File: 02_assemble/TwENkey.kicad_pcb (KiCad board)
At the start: 2 copper layers, 304.4 x 98.8 mm, 149 parts, among them J1 Conn_01x02, SW1 RotaryEncoder_Switch, SW10 SW_PUSH, SW11 SW_PUSH, SW12 SW_PUSH, SW13 SW_PUSH, SW14 SW_PUSH, SW15 SW_PUSH, SW16 SW_PUSH, SW17 SW_PUSH, SW18 SW_PUSH, SW19 SW_PUSH, SW2 SW_PUSH, SW20 SW_PUSH, SW21 SW_PUSH, SW22 SW_PUSH, SW23 SW_PUSH, SW24 SW_PUSH, SW25 SW_PUSH, SW26 SW_PUSH, SW27 SW_PUSH, SW28 SW_PUSH, SW29 SW_PUSH, SW3 SW_PUSH, SW30 SW_PUSH, SW31 SW_PUSH, SW32 SW_PUSH, SW33 SW_PUSH, SW34 SW_PUSH, SW35 SW_PUSH, SW36 SW_PUSH, SW37 SW_PUSH, SW38 SW_PUSH, SW39 SW_PUSH, SW4 SW_PUSH, SW40 SW_PUSH, SW41 SW_PUSH, SW42 SW_PUSH, SW43 SW_PUSH, SW44 SW_PUSH, SW45 SW_PUSH, SW46 SW_PUSH, SW47 SW_PUSH, SW48 SW_PUSH, SW49 SW_PUSH, SW5 SW_PUSH, SW50 SW_PUSH, SW51 SW_PUSH, SW52 SW_PUSH, SW53 SW_PUSH, SW54 SW_PUSH, SW55 SW_PUSH, SW56 SW_PUSH, SW57 SW_PUSH, SW58 SW_PUSH, SW59 SW_PUSH, SW6 SW_PUSH, SW60 SW_PUSH, SW61 SW_PUSH, SW62 SW_PUSH, SW63 SW_PUSH, SW64 SW_PUSH, SW65 SW_PUSH, SW66 SW_PUSH, SW67 SW_PUSH, SW68 SW_PUSH, SW69 SW_PUSH, SW7 SW_PUSH, SW70 SW_PUSH, SW71 SW_PUSH, SW72 SW_PUSH, SW8 SW_PUSH, SW9 SW_PUSH, U1 Micon_BLEMicroPro

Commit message: サリチル酸さんのレビューを受けて修正
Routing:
- net Row1: track 345.2 -> 384.0 mm, vias 0 -> 1
- net Row3: track 367.0 -> 395.1 mm
- net Row0: track 337.3 -> 362.4 mm, vias 2 -> 4
- net Row4: track 383.2 -> 401.0 mm
- net Row2: track 355.9 -> 372.4 mm
- net Net-(D58-Pad1): track 13.4 -> 23.3 mm
- net Net-(D69-Pad1): track 13.8 -> 19.9 mm, vias 2 -> 0
- net Net-(D63-Pad1): track 10.9 -> 16.6 mm
- net Net-(D59-Pad1): track 15.0 -> 20.3 mm
- net Net-(D70-Pad1): track 14.1 -> 18.8 mm
- net Net-(D53-Pad1): track 16.3 -> 19.9 mm
- net Net-(D60-Pad1): track 15.0 -> 18.6 mm
- net Net-(D43-Pad1): track 14.3 -> 17.4 mm
- net Col6: track 391.9 -> 394.3 mm
- net Net-(D48-Pad1): track 20.7 -> 22.6 mm
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
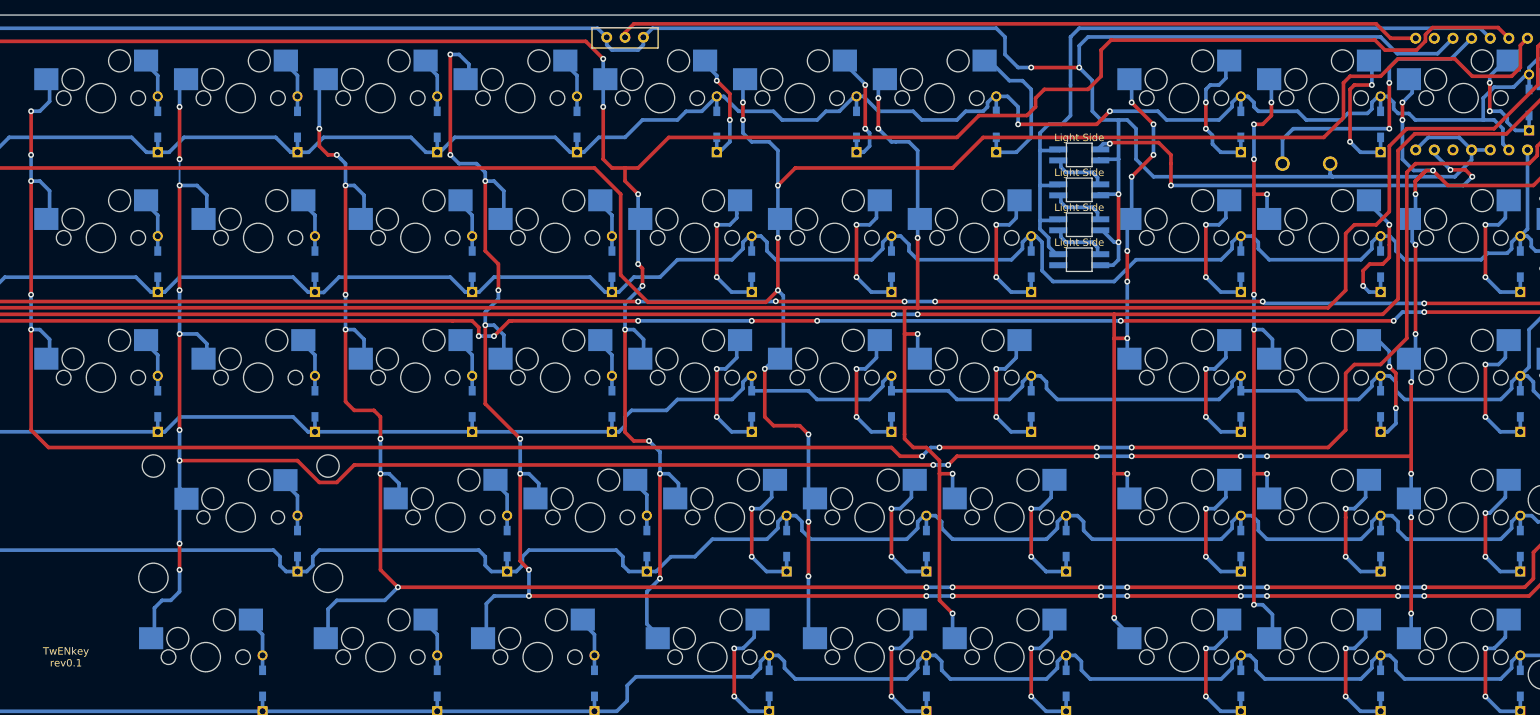
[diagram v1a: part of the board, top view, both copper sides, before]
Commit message: TRRSコネクタを追加
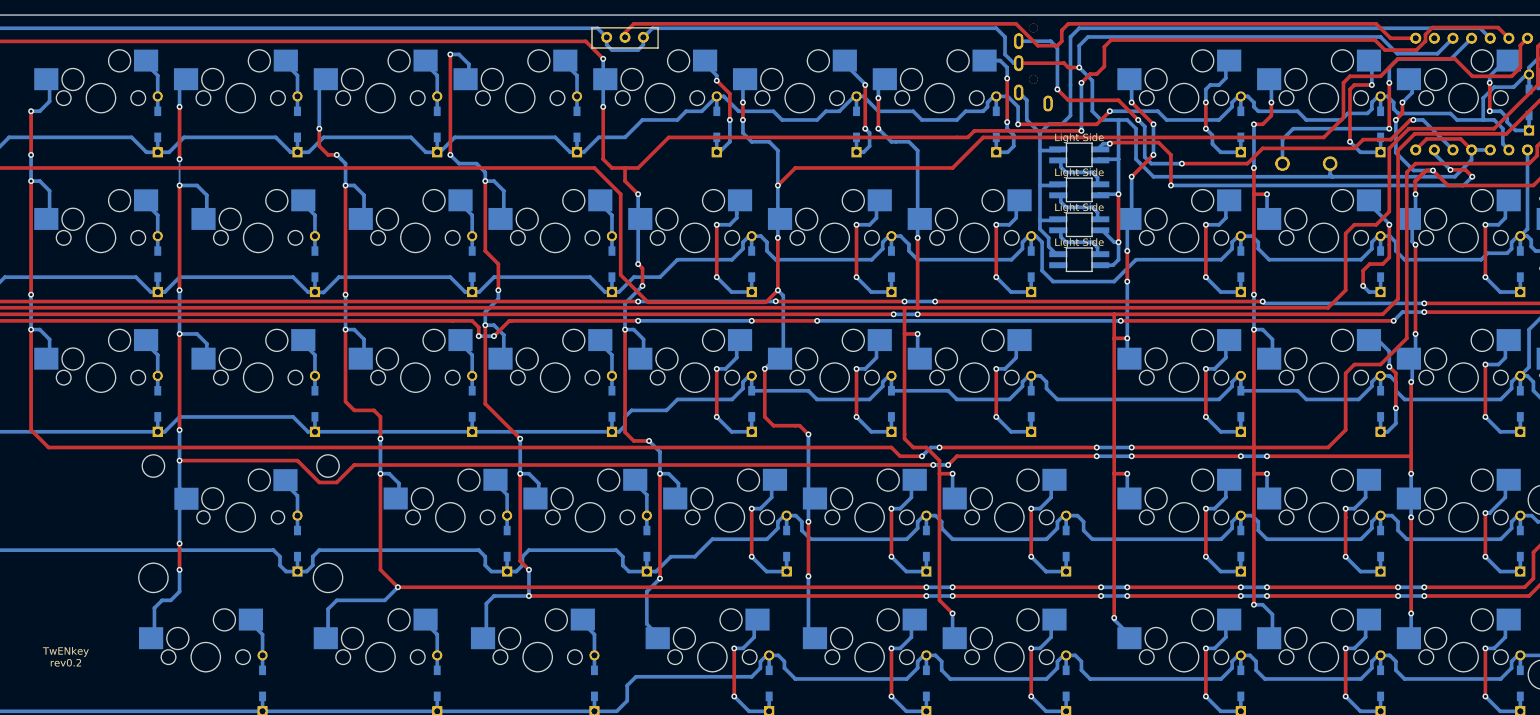
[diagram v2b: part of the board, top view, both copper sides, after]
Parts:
- added J2: MJ-4PP-9, kbd_Parts:TRRS_MJ-4PP-9, F.Cu at (236.6, 23.5)
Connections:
- U1 pad 2: unconnected-(U1-Pad2) -> Data
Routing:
- net Data: track 0.00 -> 76.0 mm, vias 0 -> 4
- net VCC: track 101.0 -> 107.7 mm
- net Bat+: track 109.7 -> 113.1 mm
- net Net-(D48-Pad1): track 22.6 -> 19.8 mm, vias 0 -> 2
- net Col0: track 469.8 -> 472.4 mm, vias 11 -> 13
- net Col5: track 391.8 -> 392.6 mm
- net GND: track 404.7 -> 404.5 mm, vias 4 -> 3
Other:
- board text added: "TwENkey rev0.2"
- board text removed: "TwENkey rev0.1"
